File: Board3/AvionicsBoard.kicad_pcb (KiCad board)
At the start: 2 copper layers, 61 parts, among them J1 USB_A, J10 I2C, J11 UART, J12 900MHz_Ant, J2 Conn_01x02, J3 SWD, J4 7.2V, J5 SPI, J6 Micro_SD_Card, J7 RF IN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

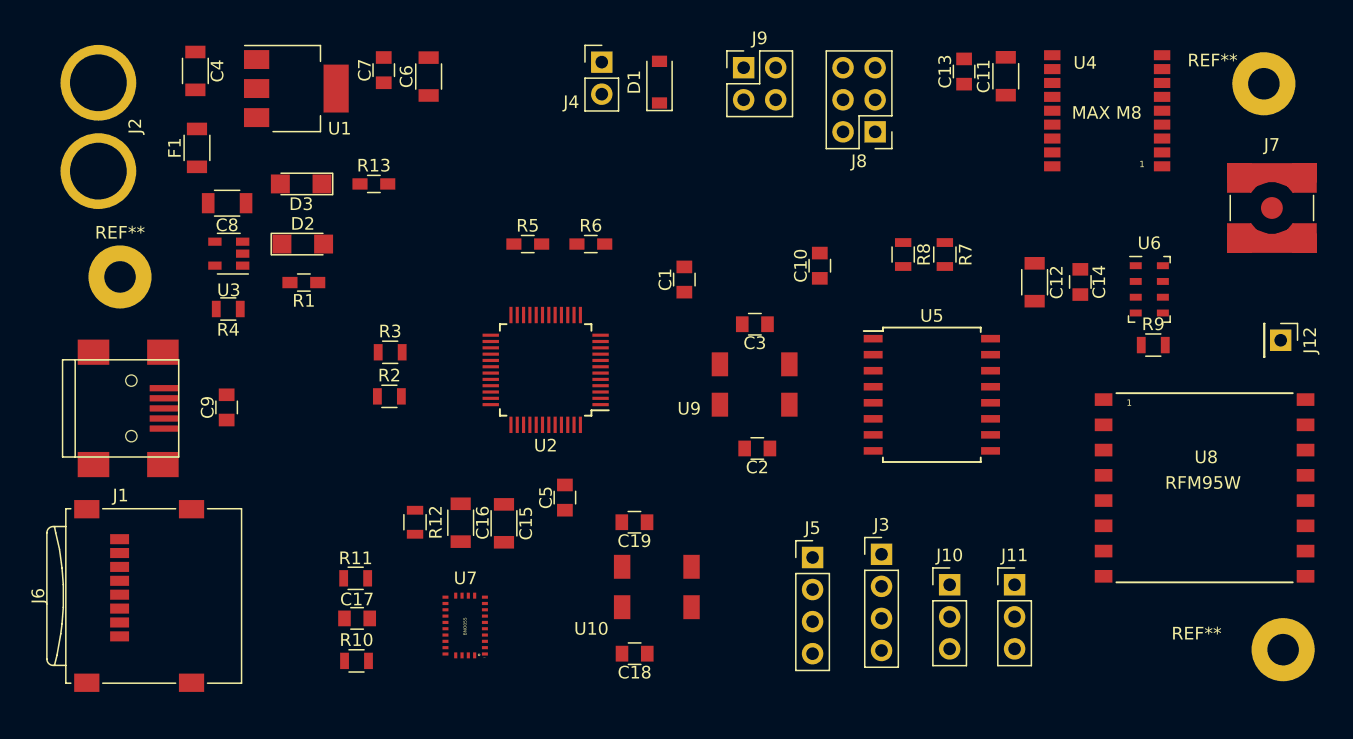
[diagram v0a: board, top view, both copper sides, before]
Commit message: Finished routing board, added logo
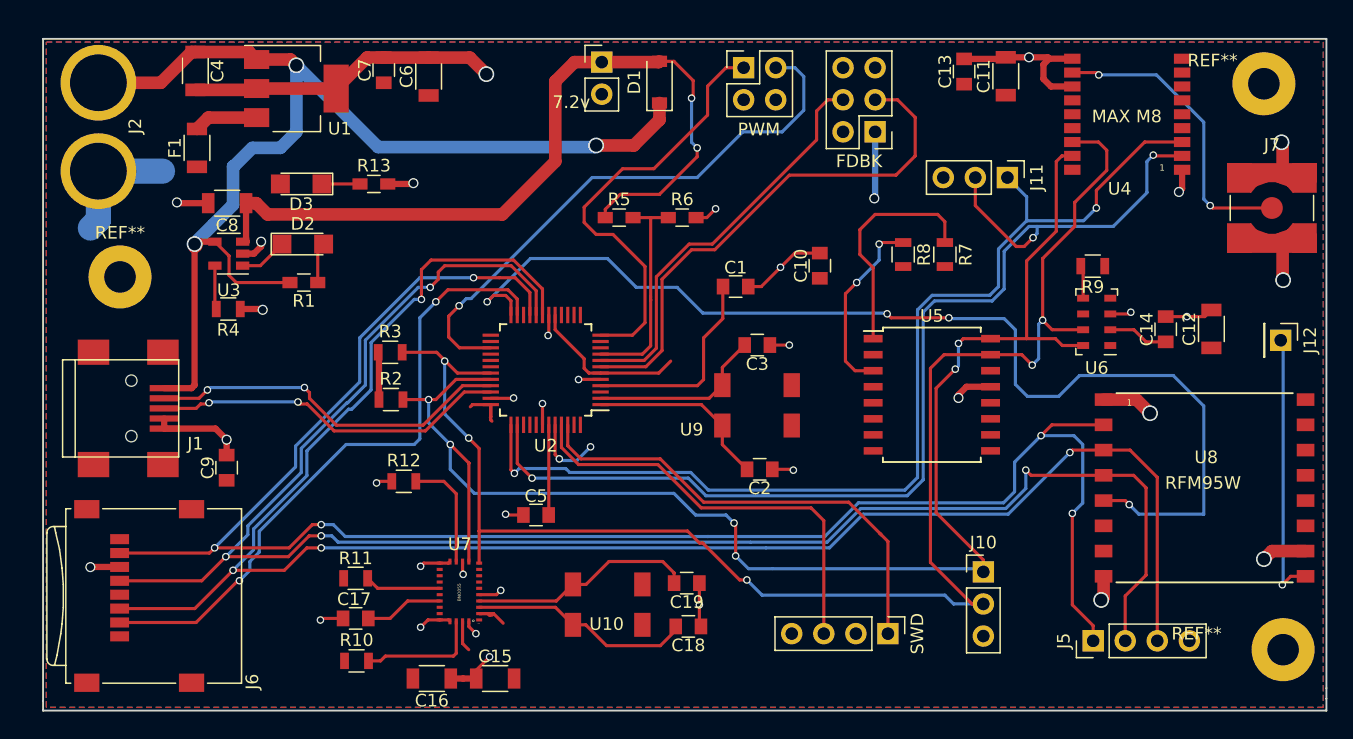
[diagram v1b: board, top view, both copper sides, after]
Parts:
- moved J11 32.3 mm to (135.6, 61.8), turned to 270 degrees
- moved J5 23.2 mm to (142.4, 98.5), turned to 90 degrees
- moved C12 14.5 mm to (151.8, 73.8), turned to 90 degrees
- moved C16 12.6 mm to (90.0, 101.5), turned to 180 degrees
- moved C15 12.3 mm to (95.1, 101.5), turned to 0 degrees
- moved R9 7.88 mm to (142.4, 68.8), turned to 180 degrees
- moved C14 7.73 mm to (148.2, 73.8), turned to 90 degrees
- moved R5 7.54 mm to (104.9, 65.0)
- moved R6 7.54 mm to (109.9, 65.0)
- moved C19 6.36 mm to (110.2, 93.9)
- moved SWD 6.31 mm to (126.2, 97.9), turned to 270 degrees
- moved U6 4.90 mm to (142.7, 73.2), turned to 180 degrees
- moved C9 4.78 mm to (73.8, 84.8)
- moved C18 4.77 mm to (110.4, 97.3)
- moved U10 4.14 mm to (101.2, 97.2)
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- renumbered J4 to 7.2v, J8 to FDBK, J9 to PWM, J3 to SWD
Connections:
- J6 pad 2: /CS -> /D2
- U2 pad 23: /CS -> /D2
- U4 pad 2: /TXD -> /RXD
- U4 pad 3: /RXD -> /TXD
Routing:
- net /MOSI: track 0.00 -> 144.8 mm, vias 0 -> 4
- net /MISO: track 0.00 -> 143.7 mm, vias 0 -> 5
- net /SCK: track 0.00 -> 140.4 mm, vias 0 -> 4
- net GND: track 0.00 -> 132.3 mm, vias 0 -> 35
- net /SDA: track 0.00 -> 123.1 mm, vias 0 -> 5
- net /SCL: track 0.00 -> 118.0 mm, vias 0 -> 6
- net VBUS: track 0.00 -> 93.4 mm, vias 0 -> 3
- net /RXD: track 0.00 -> 88.4 mm, vias 0 -> 3
- net /CS: track 0.00 -> 87.3 mm, vias 0 -> 4
- net /TXD: track 0.00 -> 83.5 mm, vias 0 -> 2
- net +7.5V: track 0.00 -> 64.5 mm, vias 0 -> 2
- net /D2: track 0.00 -> 51.0 mm, vias 0 -> 2
- net /D10: track 0.00 -> 45.4 mm, vias 0 -> 1
- net /A1: track 0.00 -> 42.0 mm
- net /SWDIO: track 0.00 -> 37.6 mm
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- added copper zone on F.Cu, net +3V3
- added copper zone on B.Cu, net GND
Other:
- board outline added: 101.7 x 53.2 mm

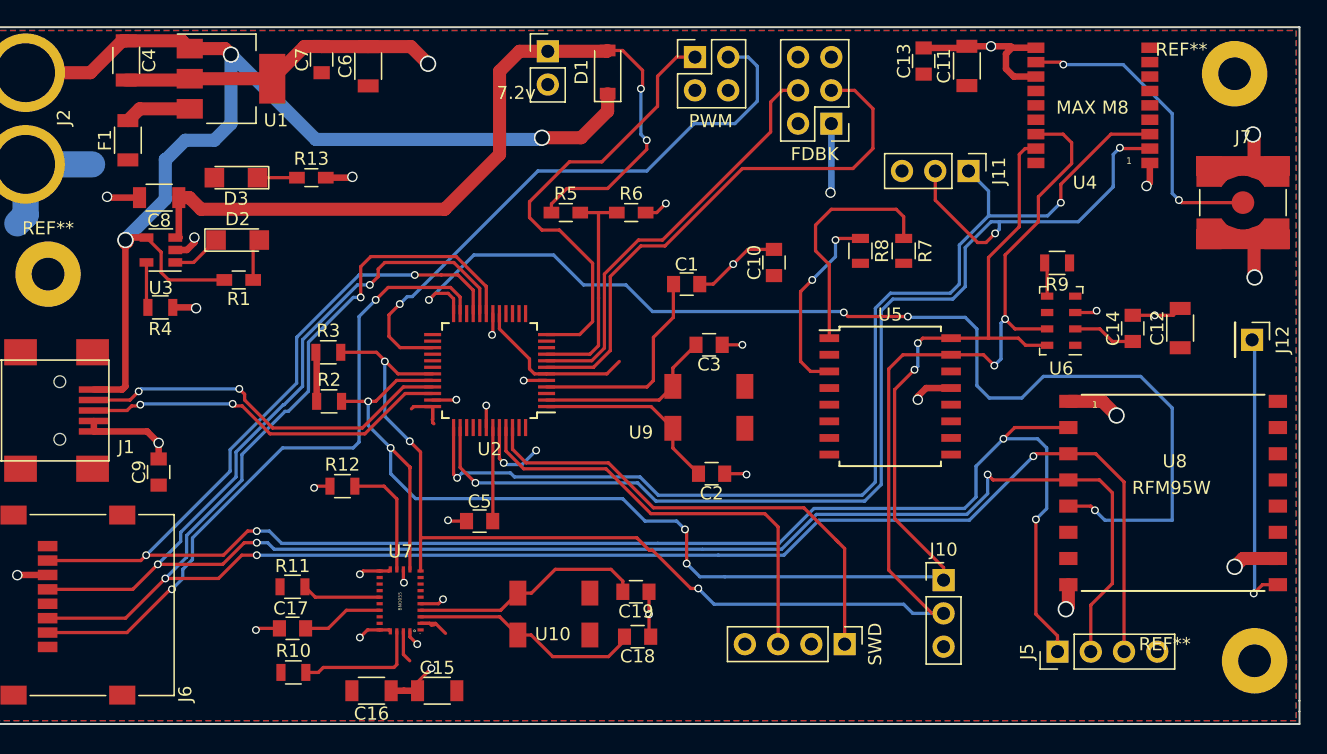
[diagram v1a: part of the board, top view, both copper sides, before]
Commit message: Fix BNO055 footprint and board layout
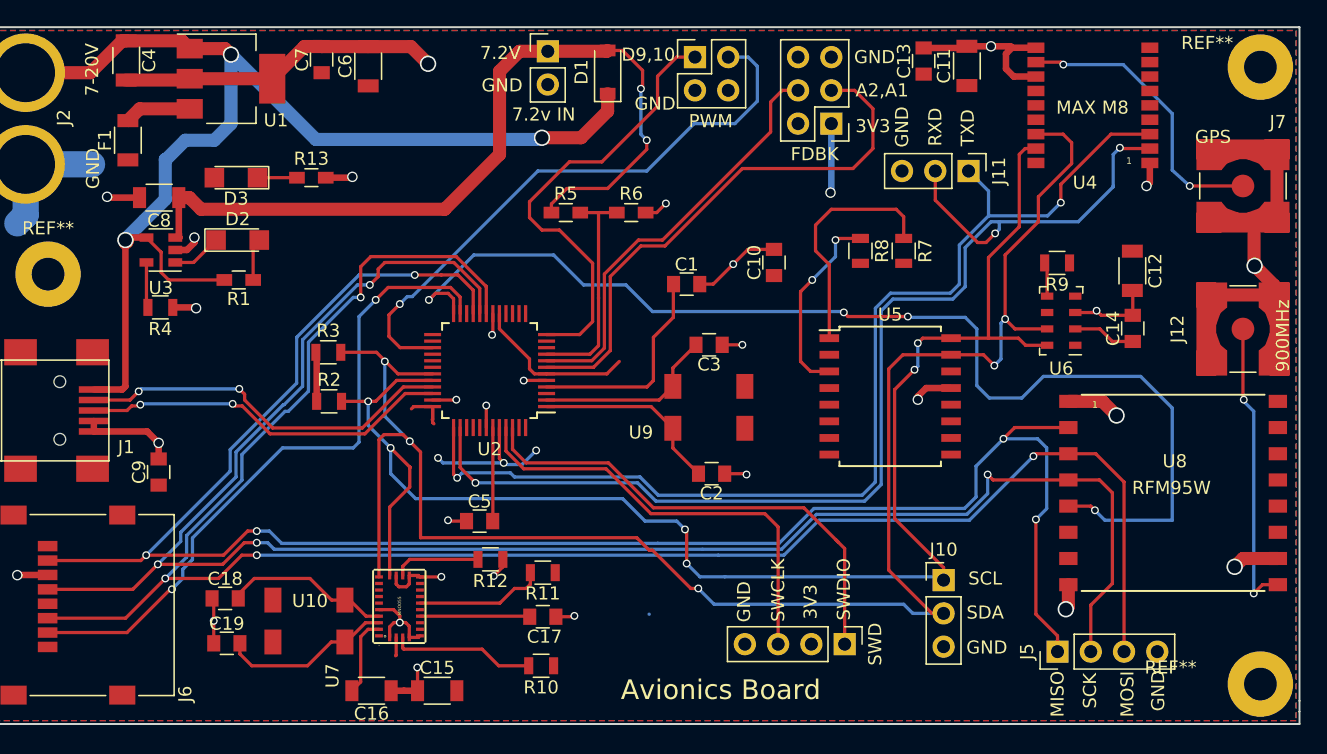
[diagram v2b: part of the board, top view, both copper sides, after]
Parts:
- added G***: LOGO, ManifestLabsLogo:Manifestabs, B.Cu at (114.6, 78.5)
- 7.2v IN: renamed from 7.2v
- J12: value 900MHz_Ant -> RF IN; footprint Pin_Headers:Pin_Header_Straight_1x01_Pitch2.54mm -> Connectors:SMA_SMD_Jack_Straight
- moved C18 31.6 mm to (78.9, 94.4), turned to 0 degrees
- moved C19 31.5 mm to (79.0, 97.9), turned to 0 degrees
- moved R11 19.1 mm to (103.1, 92.5), turned to 0 degrees
- moved C17 19.1 mm to (103.1, 95.8), turned to 0 degrees
- moved R10 18.9 mm to (103.0, 99.6), turned to 180 degrees
- moved U10 13.5 mm to (88.0, 94.6), turned to 180 degrees
- moved R12 12.6 mm to (99.1, 91.4), turned to 180 degrees
- moved U7 5.88 mm to (90.6, 97.3), turned to 90 degrees
- moved C12 5.70 mm to (148.1, 69.4), turned to 270 degrees
- moved REF** 2.03 mm to (157.9, 53.8)
- moved REF** 1.83 mm to (157.9, 101.0)
- moved J7 1.27 mm to (156.6, 62.9)
- moved J12 1.08 mm to (156.6, 73.9), turned to 90 degrees
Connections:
- C18 pad 2: /OSC_IN -> /OSC_OUT
- C19 pad 2: /OSC_OUT -> /OSC_IN
- U10 pad 1: /OSC_IN -> /OSC_OUT
- U10 pad 4: /OSC_OUT -> /OSC_IN
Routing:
- net GND: track 132.3 -> 144.6 mm, vias 35 -> 30
- net /SDA: track 123.1 -> 133.8 mm
- net +3V3: track 37.3 -> 44.1 mm, vias 3 -> 4
- net /OSC_OUT: track 17.9 -> 12.7 mm
- net /OSC_IN: track 17.6 -> 13.2 mm
- net Net-(R11-Pad1): track 6.04 -> 9.92 mm
- net Net-(R12-Pad2): track 8.99 -> 6.66 mm
- net Net-(C17-Pad1): track 6.23 -> 8.40 mm
- net Net-(J7-Pad1): track 23.8 -> 22.2 mm
- net Net-(R10-Pad2): track 9.74 -> 11.0 mm
- net Net-(J12-Pad1): track 21.6 -> 22.7 mm, vias 1 -> 2
- net /SCL: track 118.0 -> 119.1 mm
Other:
- board text added: "3V3"
- board text added: "7-20V"
- board text added: "7.2V"
- board text added: "900MHz"
- board text added: "A2,A1"
- board text added: "Avionics Board"
- board text added: "D9,10"
- board text added: "Danny Mallek 2018"
- board text added: "GND"
- board text added: "GPS"
- board text added: "MISO"
- board text added: "MOSI"
- board text added: "RXD"
- board text added: "SCK"
- board text added: "SCL"
- board text added: "SDA"
- board text added: "SWCLK"
- board text added: "SWDIO"
- board text added: "TXD"

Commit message: Little bit o PCB layout
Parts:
- removed G***: LOGO, ManifestLabsLogo:Manifestabs
- removed J12, J7: RF IN, Connectors:SMA_SMD_Jack_Straight
- added BT1: Battery_Cell, Battery_Holders:Keystone_1058_1x2032-CoinCell, B.Cu at (212.5, 74.4)
- added C20: 10u, Capacitors_SMD:C_1206, F.Cu at (180.3, 81.9)
- added C21: 10u, Capacitors_SMD:C_1206, F.Cu at (181.0, 95.2)
- added J13: RFD900 Connector, FoxWestern:RFD900, B.Cu at (170.6, 81.0)
- added R14: 0, Resistors_SMD:R_0805, F.Cu at (142.4, 37.2)
- added R15: 0, Resistors_SMD:R_0805, F.Cu at (142.4, 40.6)
- added R16: 0, Resistors_SMD:R_0805, F.Cu at (168.9, 62.2)
- added R17: 0, Resistors_SMD:R_0805, F.Cu at (168.9, 64.8)
- added R18: 0, Resistors_SMD:R_0805, F.Cu at (168.9, 69.2)
- added U11: GT-U7_GPS, FoxWestern:GPS_GT-07, F.Cu at (164.5, 59.7)
- added U12: LM340MP-5.0, TO_SOT_Packages_SMD:SOT-223-3_TabPin2, F.Cu at (181.0, 88.3)
- moved I2C 9.47 mm to (137.2, 101.9), turned to 270 degrees
- moved SWD 3.94 mm to (126.1, 101.9)
- moved SPI 3.34 mm to (142.4, 101.8)
- moved U9 2.42 mm to (110.9, 82.5)
- moved C3 2.18 mm to (114.0, 76.3)
- moved C2 1.83 mm to (114.2, 85.3)
- renumbered J10 to I2C, J5 to SPI
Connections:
- J6 pad 2: /D2 -> /D4
- U2 pad 24: /CS -> /D5
- U4 pad 2: /RXD -> Net-(R14-Pad1)
- U4 pad 3: /TXD -> Net-(R15-Pad1)
- U8 pad 5: /CS -> /D3
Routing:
- net /CS: track 87.3 -> 0.00 mm, vias 4 -> 0
- net /D3: track 0.00 -> 79.3 mm, vias 0 -> 4
- net /D4: track 0.00 -> 58.2 mm, vias 0 -> 2
- net /D2: track 51.0 -> 0.00 mm, vias 2 -> 0
- net GND: track 144.6 -> 129.9 mm, vias 30 -> 29
- net /SCL: track 119.1 -> 129.3 mm, vias 6 -> 7
- net /SDA: track 133.8 -> 139.1 mm, vias 5 -> 6
- net /SWDIO: track 37.6 -> 41.6 mm
- net /SWCLK: track 33.9 -> 37.9 mm
- net /MISO: track 143.7 -> 147.0 mm
- net /SCK: track 140.4 -> 143.8 mm
- net /MOSI: track 144.8 -> 148.2 mm
- net Net-(R15-Pad1): track 0.00 -> 2.96 mm
- net /TXD: track 83.5 -> 80.6 mm
- net Net-(R14-Pad1): track 0.00 -> 2.22 mm
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
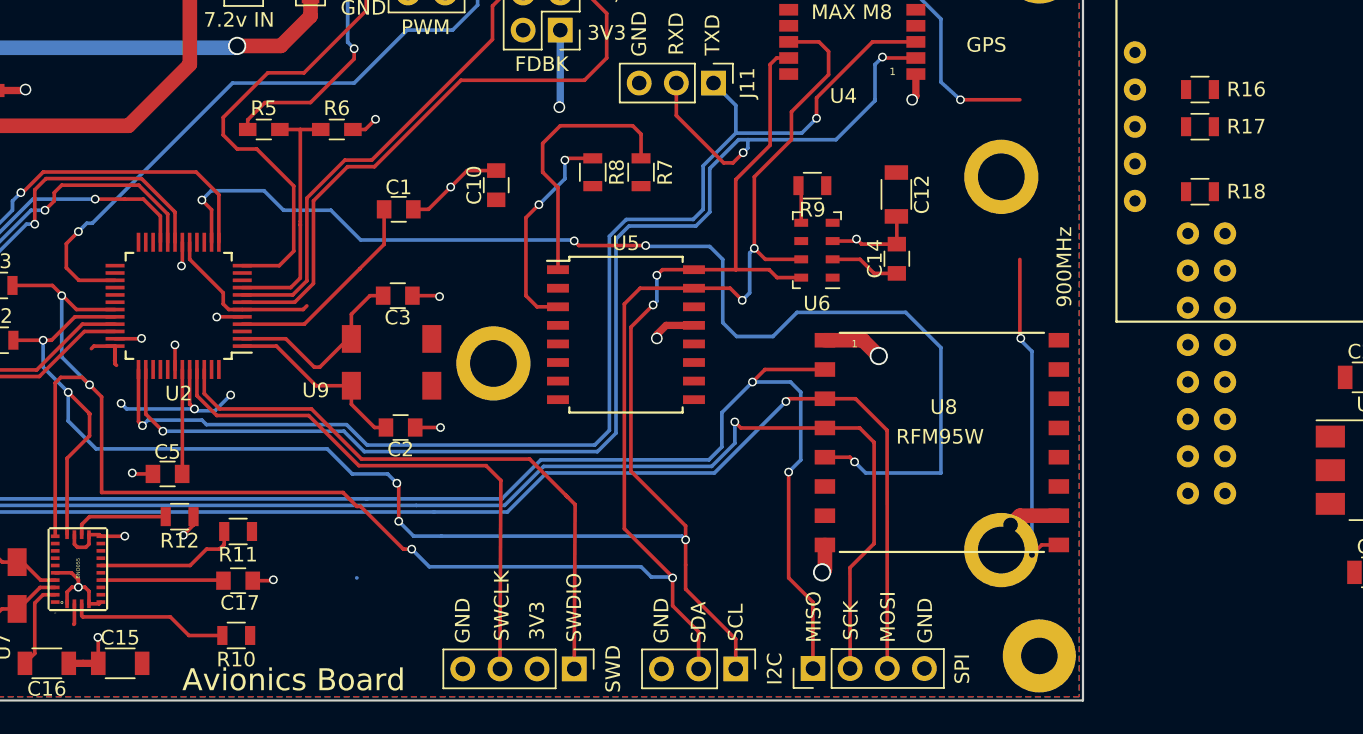
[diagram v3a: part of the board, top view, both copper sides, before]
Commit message: Get that RFD900 UART outta the uC to that radio
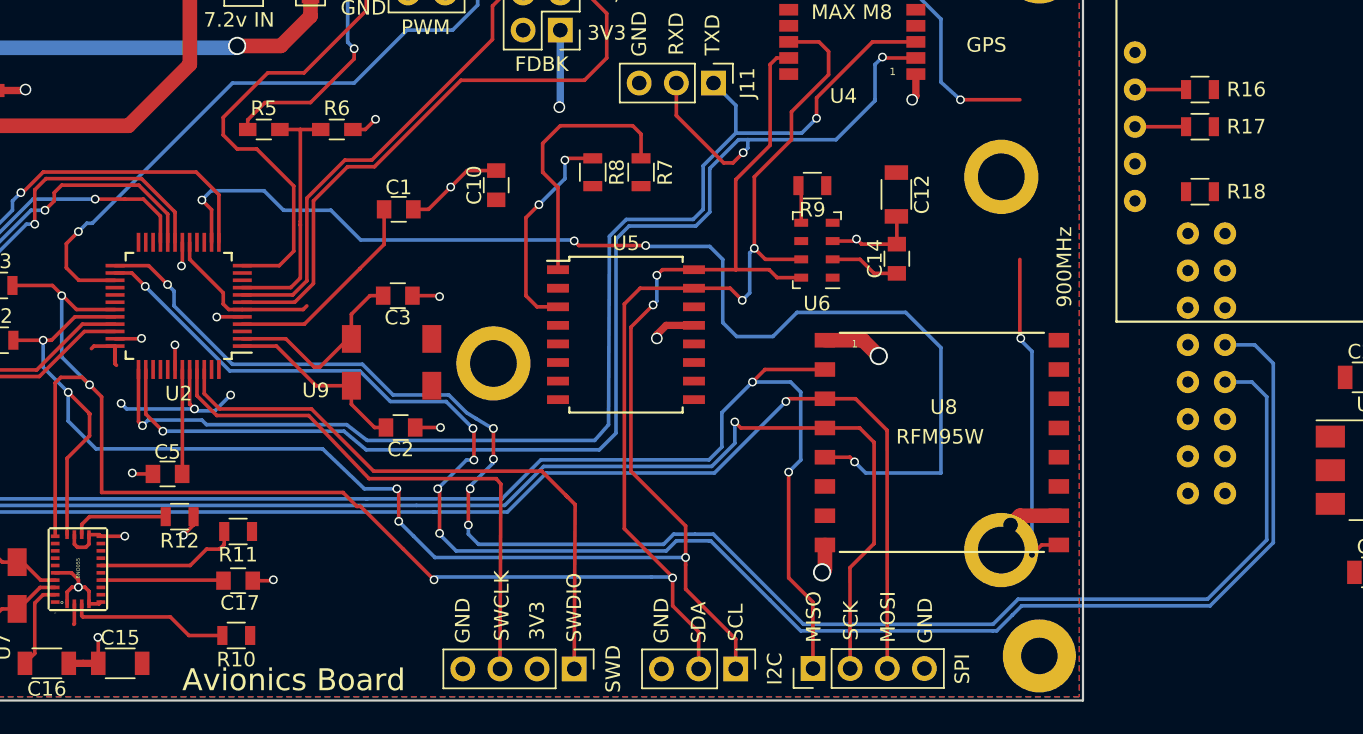
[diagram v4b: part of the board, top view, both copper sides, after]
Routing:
- net /D13: track 0.00 -> 116.4 mm, vias 0 -> 5
- net /D11: track 0.00 -> 112.1 mm, vias 0 -> 5
- net Net-(R17-Pad1): track 0.00 -> 3.50 mm
- net Net-(R16-Pad1): track 0.00 -> 3.50 mm
- net /TXD: track 80.6 -> 80.0 mm

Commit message: Make board that is too fat
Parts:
- removed BT1: Battery_Cell, Battery_Holders:Keystone_1058_1x2032-CoinCell
- added REF**: MountingHole_2.5mm_Pad, Mounting_Holes:MountingHole_2.5mm_Pad, F.Cu at (62.3, 137.1)
- added REF**: MountingHole_2.5mm_Pad, Mounting_Holes:MountingHole_2.5mm_Pad, F.Cu at (157.9, 137.1)
- J13: moved to F.Cu
- moved R16 116.7 mm to (65.8, 116.8)
- moved R17 116.7 mm to (65.8, 119.3)
- moved U11 116.7 mm to (61.3, 114.2)
- moved R18 116.7 mm to (65.8, 123.8)
- moved C21 109.0 mm to (75.8, 123.9)
- moved C20 108.5 mm to (75.7, 110.5)
- moved U12 107.5 mm to (77.4, 116.9)
- moved J13 86.0 mm to (93.3, 118.7), turned to 180 degrees
- moved R14 28.8 mm to (145.1, 65.8), turned to 180 degrees
- moved R15 23.5 mm to (145.1, 63.9), turned to 180 degrees
- moved REF** 16.1 mm to (62.3, 53.8)
- moved J2 7.14 mm to (65.2, 68.2)
- moved I2C 2.26 mm to (137.3, 99.6)
- moved SWD 2.26 mm to (126.1, 99.6)
- moved SPI 2.26 mm to (142.4, 99.6)
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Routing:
- net VBUS: track 93.4 -> 159.3 mm
- net /TXD: track 80.0 -> 129.5 mm, vias 2 -> 8
- net /RXD: track 86.0 -> 132.6 mm, vias 3 -> 9
- net +5V: track 0.00 -> 40.7 mm
- net /D13: track 116.4 -> 84.0 mm, vias 5 -> 4
- net /D11: track 112.1 -> 82.5 mm, vias 5 -> 4
- net GND: track 129.9 -> 143.8 mm, vias 29 -> 31
- net Net-(R14-Pad1): track 2.22 -> 8.51 mm
- net Net-(R15-Pad1): track 2.96 -> 7.34 mm
- net Net-(R18-Pad1): track 0.00 -> 3.76 mm
- net /SCL: track 129.6 -> 127.1 mm
- net /SWDIO: track 41.6 -> 39.3 mm
- net /SWCLK: track 38.1 -> 35.8 mm
- net /MISO: track 147.0 -> 144.8 mm
- net /MOSI: track 148.2 -> 145.9 mm
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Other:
- board size 101.7 x 53.2 mm -> 101.9 x 89.2 mm
- board text added: "Avionics + Telemetery System"

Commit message: Create skinny boi
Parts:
- added REF**: MountingHole_2.5mm_Pad, Mounting_Holes:MountingHole_2.5mm_Pad, F.Cu at (213.4, 106.7)
- J13: moved to B.Cu
- moved J13 130.3 mm to (215.0, 71.9), turned to 0 degrees
- moved U12 106.8 mm to (181.5, 93.4)
- moved C20 106.8 mm to (179.8, 87.0)
- moved C21 106.8 mm to (179.9, 100.4)
- moved R16 106.8 mm to (169.9, 93.3)
- moved R17 106.8 mm to (169.9, 95.8)
- moved R18 106.8 mm to (169.9, 100.2)
- moved U11 106.8 mm to (165.5, 90.7)
- moved REF** 100.0 mm to (213.3, 53.8)
- moved REF** 30.6 mm to (62.2, 106.5)
- moved REF** 7.62 mm to (157.9, 106.7)
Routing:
- net /D13: track 84.0 -> 156.9 mm, vias 4 -> 7
- net /D11: track 82.5 -> 154.0 mm, vias 4 -> 6
- net VBUS: track 159.3 -> 221.7 mm, vias 3 -> 9
- net Net-(J12-Pad1): track 22.7 -> 2.21 mm, vias 2 -> 1
- net GND: track 143.8 -> 156.4 mm, vias 31 -> 33
- net +5V: track 40.7 -> 52.9 mm
- net /RXD: track 132.6 -> 127.5 mm, vias 9 -> 4
- net /TXD: track 129.5 -> 132.6 mm, vias 8 -> 3
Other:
- board size 101.9 x 89.2 mm -> 157.4 x 59 mm
